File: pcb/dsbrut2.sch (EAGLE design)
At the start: 17 parts, among them IC1 4175D, IC2 74HC125D, IC3 MEGA8-AI

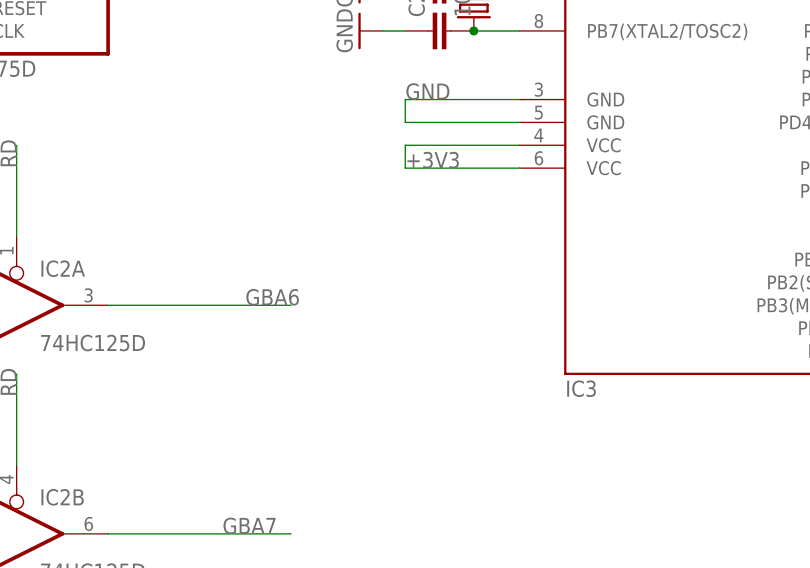
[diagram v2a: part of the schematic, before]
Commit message: added c3 between vcc and gnd, moved c2 away from steg
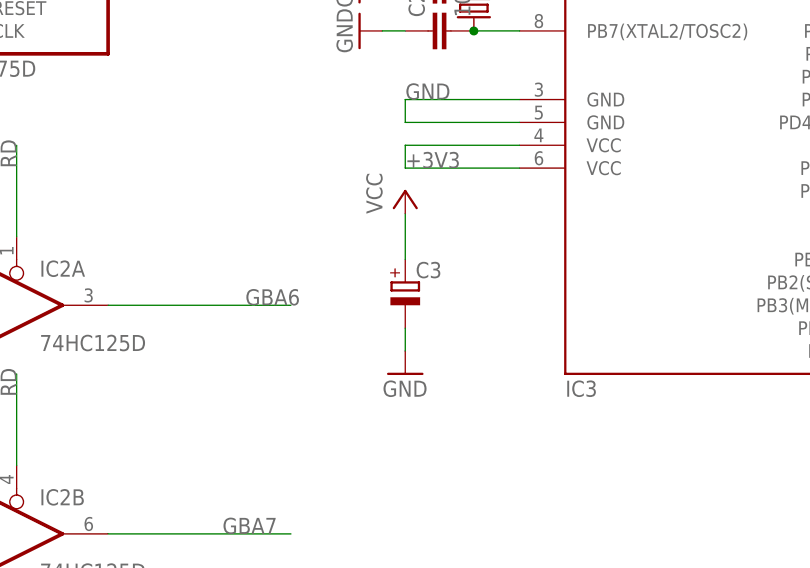
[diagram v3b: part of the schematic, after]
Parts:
- added C3: (no value), rcl:CPOL-EUSMCA
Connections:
- net +3V3: now also C3.+
- net GND: now also C3.-
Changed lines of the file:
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@@
 <grid distance="0.1" unitdist="inch" unit="inch" style="lines" multiple="1" display="no" altdistance="0.01" altunitdist="inch" altunit="inch"/>
 <layers>
-<layer number="1" name="Top" color="4" fill="1" visible="no" active="no"/>
-<layer number="16" name="Bottom" color="1" fill="1" visible="no" active="no"/>
-<layer number="17" name="Pads" color="2" fill="1" visible="no" active="no"/>
-<layer number="18" name="Vias" color="2" fill="1" visible="no" active="no"/>
-<layer number="19" name="Unrouted" color="6" fill="1" visible="no" active="no"/>
-<layer number="20" name="Dimension" color="15" fill="1" visible="no" active="no"/>
-<layer number="21" name="tPlace" color="7" fill="1" visible="no" active="no"/>
-<layer number="22" name="bPlace" color="7" fill="1" visible="no" active="no"/>
-<layer number="23" name="tOrigins" color="15" fill="1" visible="no" active="no"/>
-<layer number="24" name="bOrigins" color="15" fill="1" visible="no" active="no"/>
-<layer number="25" name="tNames" color="7" fill="1" visible="no" active="no"/>
-<layer number="26" name="bNames" color="7" fill="1" visible="no" active="no"/>
-<layer number="27" name="tValues" color="7" fill="1" visible="no" active="no"/>
-<layer number="28" name="bValues" color="7" fill="1" visible="no" active="no"/>
+<layer number="1" name="Top" color="4" fill="1" visible="yes" active="no"/>
+<layer number="16" name="Bottom" color="1" fill="1" visible="yes" active="no"/>
+<layer number="17" name="Pads" color="2" fill="1" visible="yes" active="no"/>
+<layer number="18" name="Vias" color="2" fill="1" visible="yes" active="no"/>
+<layer number="19" name="Unrouted" color="6" fill="1" visible="yes" active="no"/>
+<layer number="20" name="Dimension" color="15" fill="1" visible="yes" active="no"/>
+<layer number="21" name="tPlace" color="7" fill="1" visible="yes" active="no"/>
+<layer number="22" name="bPlace" color="7" fill="1" visible="yes" active="no"/>
+<layer number="23" name="tOrigins" color="15" fill="1" visible="yes" active="no"/>
+<layer number="24" name="bOrigins" color="15" fill="1" visible="yes" active="no"/>
+<layer number="25" name="tNames" color="7" fill="1" visible="yes" active="no"/>
+<layer number="26" name="bNames" color="7" fill="1" visible="yes" active="no"/>
+<layer number="27" name="tValues" color="7" fill="1" visible="yes" active="no"/>
+<layer number="28" name="bValues" color="7" fill="1" visible="yes" active="no"/>
 <layer number="29" name="tStop" color="7" fill="3" visible="no" active="no"/>
 <layer number="30" name="bStop" color="7" fill="6" visible="no" active="no"/>
@@
 <layer number="35" name="tGlue" color="7" fill="4" visible="no" active="no"/>
 <layer number="36" name="bGlue" color="7" fill="5" visible="no" active="no"/>
-<layer number="37" name="tTest" color="7" fill="1" visible="no" active="no"/>
-<layer number="38" name="bTest" color="7" fill="1" visible="no" active="no"/>
+<layer number="37" name="tTest" color="7" fill="1" visible="yes" active="no"/>
+<layer number="38" name="bTest" color="7" fill="1" visible="yes" active="no"/>
 <layer number="39" name="tKeepout" color="4" fill="11" visible="no" active="no"/>
 <layer number="40" name="bKeepout" color="1" fill="11" visible="no" active="no"/>
@@
 <layer number="44" name="Drills" color="7" fill="1" visible="no" active="no"/>
 <layer number="45" name="Holes" color="7" fill="1" visible="no" active="no"/>
-<layer number="46" name="Milling" color="3" fill="1" visible="no" active="no"/>
-<layer number="47" name="Measures" color="7" fill="1" visible="no" active="no"/>
-<layer number="48" name="Document" color="7" fill="1" visible="no" active="no"/>
-<layer number="49" name="Reference" color="7" fill="1" visible="no" active="no"/>
-<layer number="50" name="dxf" color="7" fill="1" visible="no" active="no"/>
-<layer number="51" name="tDocu" color="7" fill="1" visible="no" active="no"/>
-<layer number="52" name="bDocu" color="7" fill="1" visible="no" active="no"/>
-<layer number="53" name="tGND_GNDA" color="7" fill="9" visible="no" active="no"/>
-<layer number="54" name="bGND_GNDA" color="1" fill="9" visible="no" active="no"/>
-<layer number="56" name="wert" color="7" fill="1" visible="no" active="no"/>
+<layer number="46" name="Milling" color="3" fill="1" visible="yes" active="no"/>
+<layer number="47" name="Measures" color="7" fill="1" visible="yes" active="no"/>
+<layer number="48" name="Document" color="7" fill="1" visible="yes" active="no"/>
+<layer number="49" name="Reference" color="7" fill="1" visible="yes" active="no"/>
+<layer number="50" name="dxf" color="7" fill="1" visible="yes" active="no"/>
+<layer number="51" name="tDocu" color="7" fill="1" visible="yes" active="no"/>
+<layer number="52" name="bDocu" color="7" fill="1" visible="yes" active="no"/>
+<layer number="53" name="tGND_GNDA" color="7" fill="9" visible="yes" active="no"/>
+<layer number="54" name="bGND_GNDA" color="1" fill="9" visible="yes" active="no"/>
+<layer number="56" name="wert" color="7" fill="1" visible="yes" active="no"/>
 <layer number="91" name="Nets" color="2" fill="1" visible="yes" active="yes"/>
 <layer number="92" name="Busses" color="1" fill="1" visible="yes" active="yes"/>
@@
 <part name="GND2" library="supply1" deviceset="GND" device=""/>
 <part name="GND4" library="supply1" deviceset="GND" device=""/>
+<part name="GND5" library="supply1" deviceset="GND" device=""/>
+<part name="P+2" library="supply1" deviceset="VCC" device=""/>
+<part name="C3" library="rcl" deviceset="CPOL-EU" device="SMCA"/>
 </parts>
 <sheets>
@@
 <instance part="GND2" gate="1" x="91.44" y="132.08" rot="R270"/>
 <instance part="GND4" gate="1" x="91.44" y="127" rot="R270"/>
+<instance part="GND5" gate="1" x="96.52" y="88.9"/>
+<instance part="P+2" gate="VCC" x="96.52" y="109.22"/>
+<instance part="C3" gate="G$1" x="96.52" y="99.06"/>
 </instances>
 <busses>
@@
 <label x="205.74" y="60.96" size="1.778" layer="95" rot="R270"/>
 </segment>
+<segment>
+<pinref part="P+2" gate="VCC" pin="VCC"/>
+<wire x1="96.52" y1="106.68" x2="96.52" y2="101.6" width="0.1524" layer="91"/>
+<pinref part="C3" gate="G$1" pin="+"/>
+</segment>
 </net>
 <net name="PD1" class="0">
@@
 <wire x1="93.98" y1="127" x2="96.52" y2="127" width="0.1524" layer="91"/>
 </segment>
-</net>
+<segment>
+<pinref part="GND5" gate="1" pin="GND"/>
+<wire x1="96.52" y1="93.98" x2="96.52" y2="91.44" width="0.1524" layer="91"/>
+<pinref part="C3" gate="G$1" pin="-"/>
+</segment>
+</net>

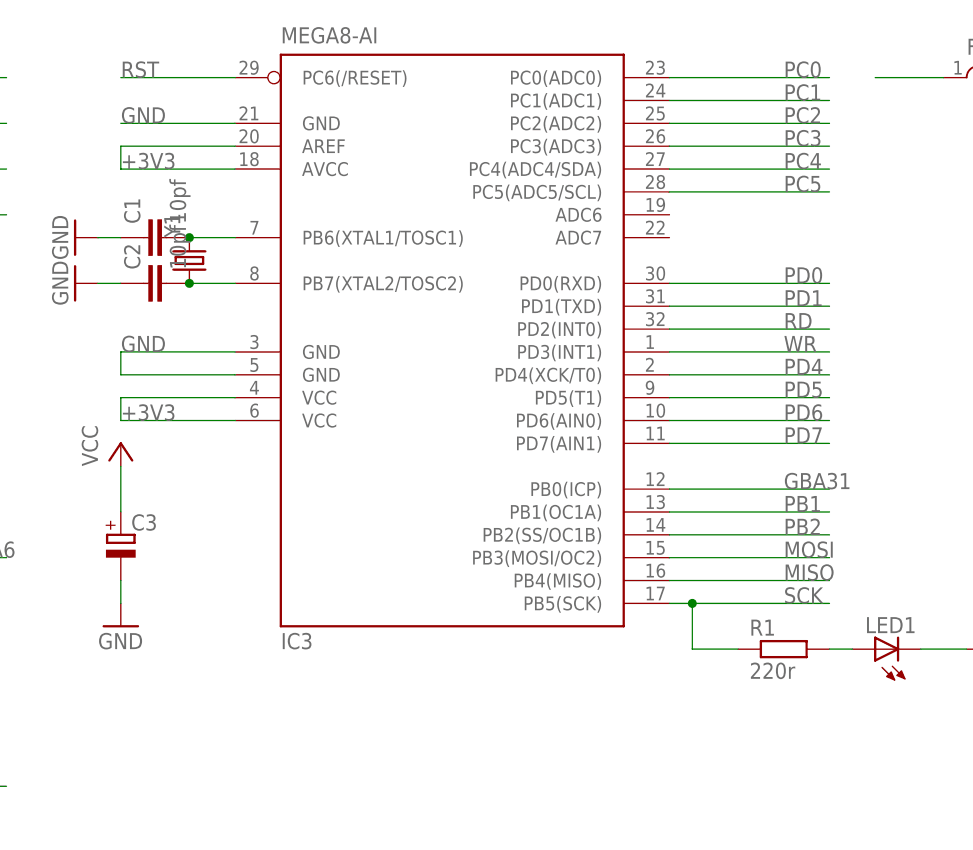
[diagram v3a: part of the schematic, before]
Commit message: Label Xtal caps as 18uF, moving a few labels
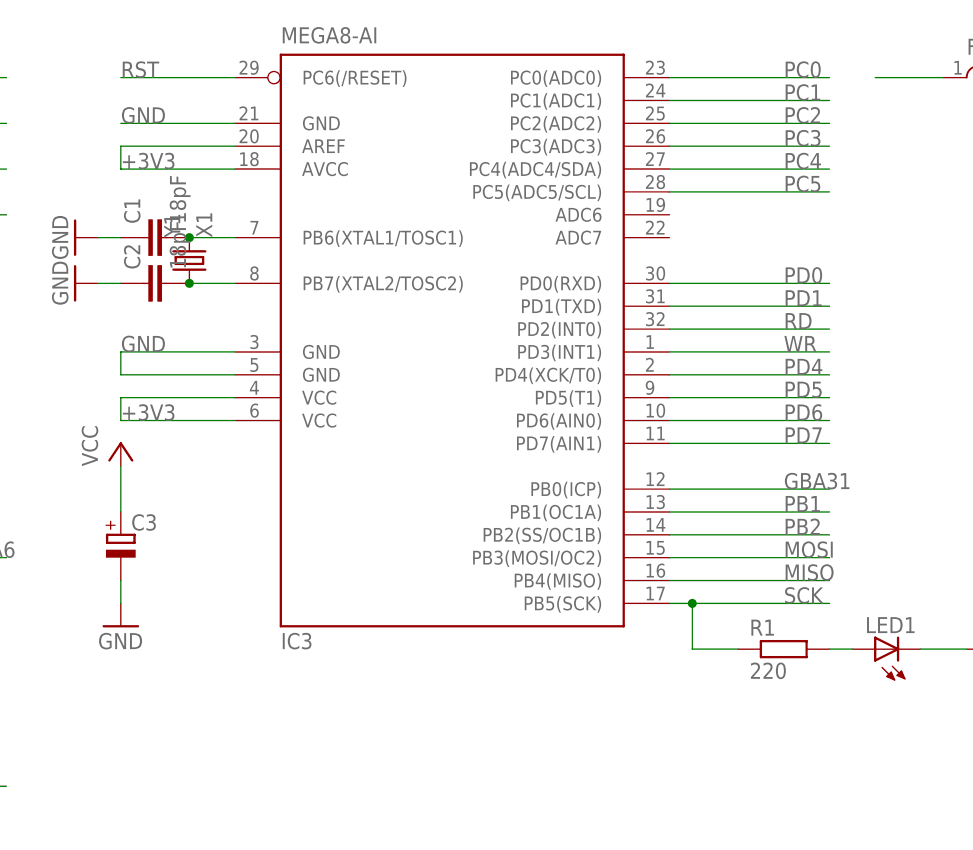
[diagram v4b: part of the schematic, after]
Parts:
- C1, C2: value 10pf -> 18pF
- R1: value 220r -> 220
- Y1: value (none) -> X1
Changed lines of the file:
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@@
 <grid distance="0.1" unitdist="inch" unit="inch" style="lines" multiple="1" display="no" altdistance="0.01" altunitdist="inch" altunit="inch"/>
 <layers>
-<layer number="1" name="Top" color="4" fill="1" visible="yes" active="no"/>
-<layer number="16" name="Bottom" color="1" fill="1" visible="yes" active="no"/>
-<layer number="17" name="Pads" color="2" fill="1" visible="yes" active="no"/>
-<layer number="18" name="Vias" color="2" fill="1" visible="yes" active="no"/>
-<layer number="19" name="Unrouted" color="6" fill="1" visible="yes" active="no"/>
-<layer number="20" name="Dimension" color="15" fill="1" visible="yes" active="no"/>
-<layer number="21" name="tPlace" color="7" fill="1" visible="yes" active="no"/>
-<layer number="22" name="bPlace" color="7" fill="1" visible="yes" active="no"/>
-<layer number="23" name="tOrigins" color="15" fill="1" visible="yes" active="no"/>
-<layer number="24" name="bOrigins" color="15" fill="1" visible="yes" active="no"/>
-<layer number="25" name="tNames" color="7" fill="1" visible="yes" active="no"/>
-<layer number="26" name="bNames" color="7" fill="1" visible="yes" active="no"/>
-<layer number="27" name="tValues" color="7" fill="1" visible="yes" active="no"/>
-<layer number="28" name="bValues" color="7" fill="1" visible="yes" active="no"/>
+<layer number="1" name="Top" color="4" fill="1" visible="no" active="no"/>
+<layer number="16" name="Bottom" color="1" fill="1" visible="no" active="no"/>
+<layer number="17" name="Pads" color="2" fill="1" visible="no" active="no"/>
+<layer number="18" name="Vias" color="2" fill="1" visible="no" active="no"/>
+<layer number="19" name="Unrouted" color="6" fill="1" visible="no" active="no"/>
+<layer number="20" name="Dimension" color="15" fill="1" visible="no" active="no"/>
+<layer number="21" name="tPlace" color="7" fill="1" visible="no" active="no"/>
+<layer number="22" name="bPlace" color="7" fill="1" visible="no" active="no"/>
+<layer number="23" name="tOrigins" color="15" fill="1" visible="no" active="no"/>
+<layer number="24" name="bOrigins" color="15" fill="1" visible="no" active="no"/>
+<layer number="25" name="tNames" color="7" fill="1" visible="no" active="no"/>
+<layer number="26" name="bNames" color="7" fill="1" visible="no" active="no"/>
+<layer number="27" name="tValues" color="7" fill="1" visible="no" active="no"/>
+<layer number="28" name="bValues" color="7" fill="1" visible="no" active="no"/>
 <layer number="29" name="tStop" color="7" fill="3" visible="no" active="no"/>
 <layer number="30" name="bStop" color="7" fill="6" visible="no" active="no"/>
@@
 <layer number="35" name="tGlue" color="7" fill="4" visible="no" active="no"/>
 <layer number="36" name="bGlue" color="7" fill="5" visible="no" active="no"/>
-<layer number="37" name="tTest" color="7" fill="1" visible="yes" active="no"/>
-<layer number="38" name="bTest" color="7" fill="1" visible="yes" active="no"/>
+<layer number="37" name="tTest" color="7" fill="1" visible="no" active="no"/>
+<layer number="38" name="bTest" color="7" fill="1" visible="no" active="no"/>
 <layer number="39" name="tKeepout" color="4" fill="11" visible="no" active="no"/>
 <layer number="40" name="bKeepout" color="1" fill="11" visible="no" active="no"/>
@@
 <layer number="44" name="Drills" color="7" fill="1" visible="no" active="no"/>
 <layer number="45" name="Holes" color="7" fill="1" visible="no" active="no"/>
-<layer number="46" name="Milling" color="3" fill="1" visible="yes" active="no"/>
-<layer number="47" name="Measures" color="7" fill="1" visible="yes" active="no"/>
-<layer number="48" name="Document" color="7" fill="1" visible="yes" active="no"/>
-<layer number="49" name="Reference" color="7" fill="1" visible="yes" active="no"/>
-<layer number="50" name="dxf" color="7" fill="1" visible="yes" active="no"/>
-<layer number="51" name="tDocu" color="7" fill="1" visible="yes" active="no"/>
-<layer number="52" name="bDocu" color="7" fill="1" visible="yes" active="no"/>
-<layer number="53" name="tGND_GNDA" color="7" fill="9" visible="yes" active="no"/>
-<layer number="54" name="bGND_GNDA" color="1" fill="9" visible="yes" active="no"/>
-<layer number="56" name="wert" color="7" fill="1" visible="yes" active="no"/>
+<layer number="46" name="Milling" color="3" fill="1" visible="no" active="no"/>
+<layer number="47" name="Measures" color="7" fill="1" visible="no" active="no"/>
+<layer number="48" name="Document" color="7" fill="1" visible="no" active="no"/>
+<layer number="49" name="Reference" color="7" fill="1" visible="no" active="no"/>
+<layer number="50" name="dxf" color="7" fill="1" visible="no" active="no"/>
+<layer number="51" name="tDocu" color="7" fill="1" visible="no" active="no"/>
+<layer number="52" name="bDocu" color="7" fill="1" visible="no" active="no"/>
+<layer number="53" name="tGND_GNDA" color="7" fill="9" visible="no" active="no"/>
+<layer number="54" name="bGND_GNDA" color="1" fill="9" visible="no" active="no"/>
+<layer number="56" name="wert" color="7" fill="1" visible="no" active="no"/>
 <layer number="91" name="Nets" color="2" fill="1" visible="yes" active="yes"/>
 <layer number="92" name="Busses" color="1" fill="1" visible="yes" active="yes"/>
@@
 <part name="LED1" library="SparkFunEagle-6-6-07" deviceset="LED" device="0603"/>
 <part name="GND3" library="supply1" deviceset="GND" device=""/>
-<part name="R1" library="rcl" deviceset="R-EU_" device="M0805" value="220r"/>
+<part name="R1" library="rcl" deviceset="R-EU_" device="M0805" value="220"/>
 <part name="VSS1" library="supply1" deviceset="VSS" device=""/>
 <part name="F1" library="dp_devices" deviceset="INDUCTOR" device="-L1812" value="F1"/>
 <part name="VDD1" library="supply1" deviceset="VDD" device=""/>
-<part name="Y1" library="SparkFun-FreqCtrl" deviceset="CRYSTAL" device="5X3"/>
-<part name="C1" library="rcl" deviceset="C-EU" device="C0603K" value="10pf"/>
-<part name="C2" library="rcl" deviceset="C-EU" device="C0603K" value="10pf"/>
+<part name="Y1" library="SparkFun-FreqCtrl" deviceset="CRYSTAL" device="5X3" value="X1"/>
+<part name="C1" library="rcl" deviceset="C-EU" device="C0603K" value="18pF"/>
+<part name="C2" library="rcl" deviceset="C-EU" device="C0603K" value="18pF"/>
 <part name="GND2" library="supply1" deviceset="GND" device=""/>
 <part name="GND4" library="supply1" deviceset="GND" device=""/>

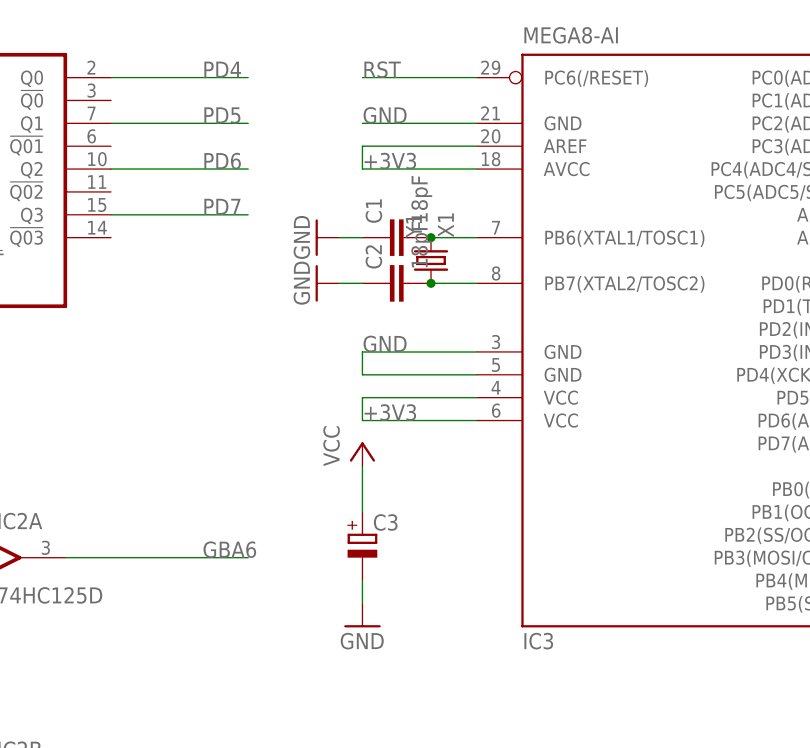
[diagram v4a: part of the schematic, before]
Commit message: Changed 18pF to 8pF, labeled C3 as 10uF
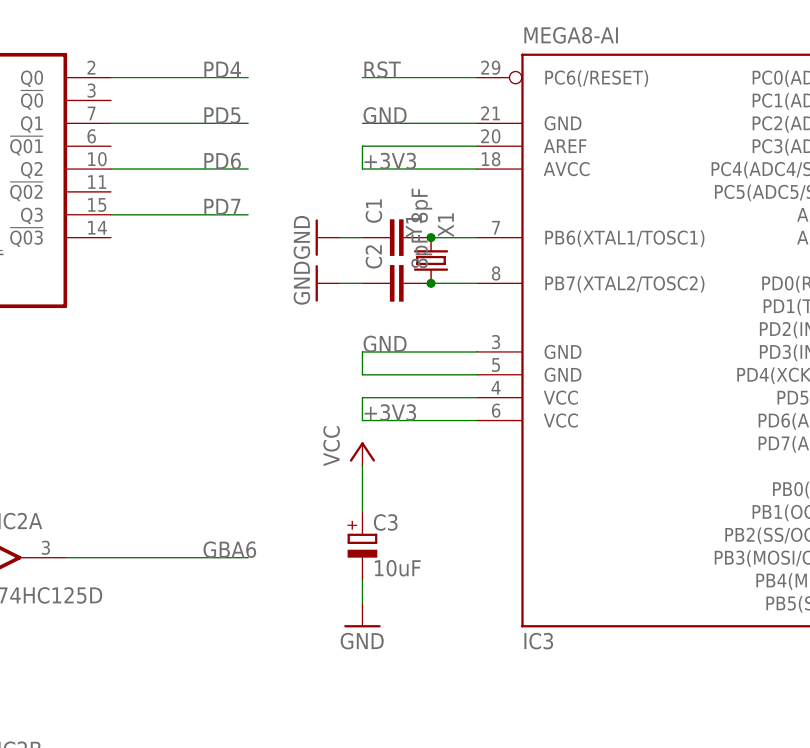
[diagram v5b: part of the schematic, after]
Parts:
- C1, C2: value 18pF -> 8pF
- C3: value (none) -> 10uF
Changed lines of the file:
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@@
 <part name="VDD1" library="supply1" deviceset="VDD" device=""/>
 <part name="Y1" library="SparkFun-FreqCtrl" deviceset="CRYSTAL" device="5X3" value="X1"/>
-<part name="C1" library="rcl" deviceset="C-EU" device="C0603K" value="18pF"/>
-<part name="C2" library="rcl" deviceset="C-EU" device="C0603K" value="18pF"/>
+<part name="C1" library="rcl" deviceset="C-EU" device="C0603K" value="8pF"/>
+<part name="C2" library="rcl" deviceset="C-EU" device="C0603K" value="8pF"/>
 <part name="GND2" library="supply1" deviceset="GND" device=""/>
 <part name="GND4" library="supply1" deviceset="GND" device=""/>
 <part name="GND5" library="supply1" deviceset="GND" device=""/>
 <part name="P+2" library="supply1" deviceset="VCC" device=""/>
-<part name="C3" library="rcl" deviceset="CPOL-EU" device="SMCA"/>
+<part name="C3" library="rcl" deviceset="CPOL-EU" device="SMCA" value="10uF"/>
 </parts>
 <sheets>
